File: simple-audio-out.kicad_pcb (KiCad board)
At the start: 2 copper layers, 49.5 x 72.4 mm, 12 parts, among them J1 Conn_01x04, Q1 2N3904

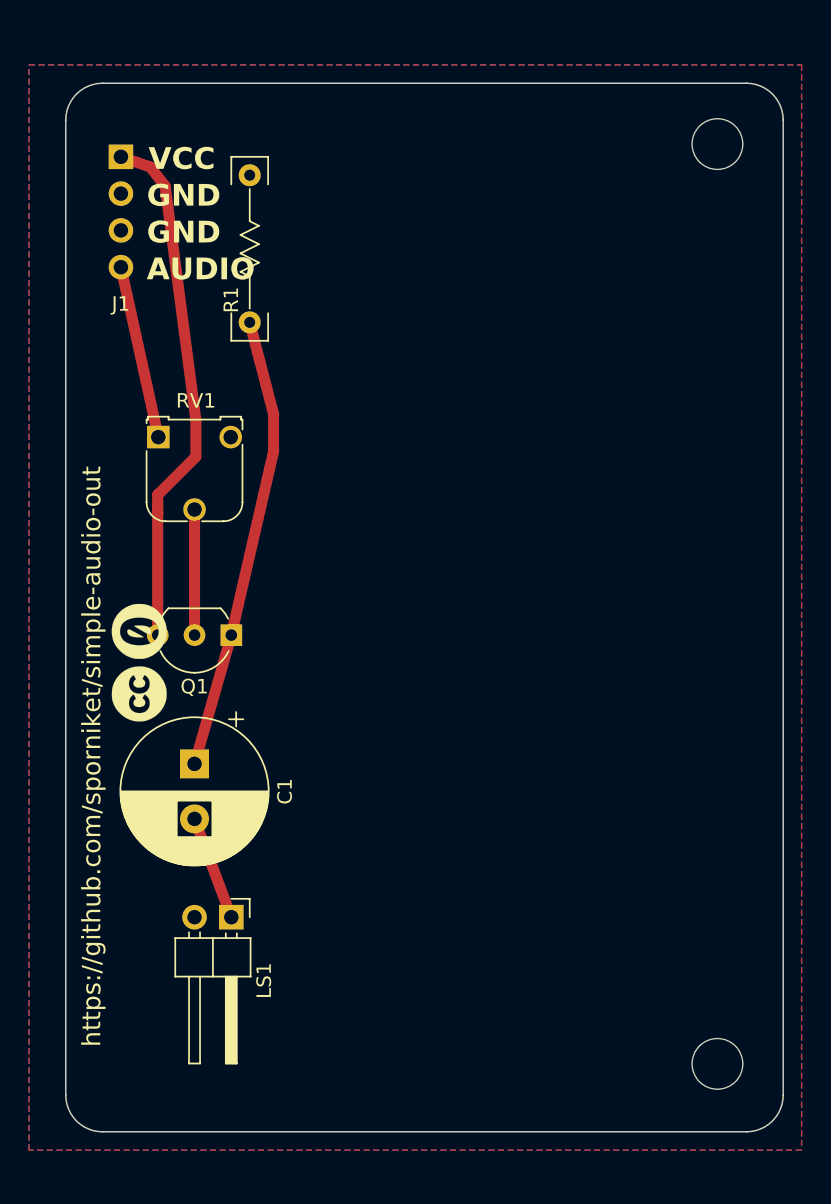
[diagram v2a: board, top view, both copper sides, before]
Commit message: #1 -- labels with project title, issue date, revision
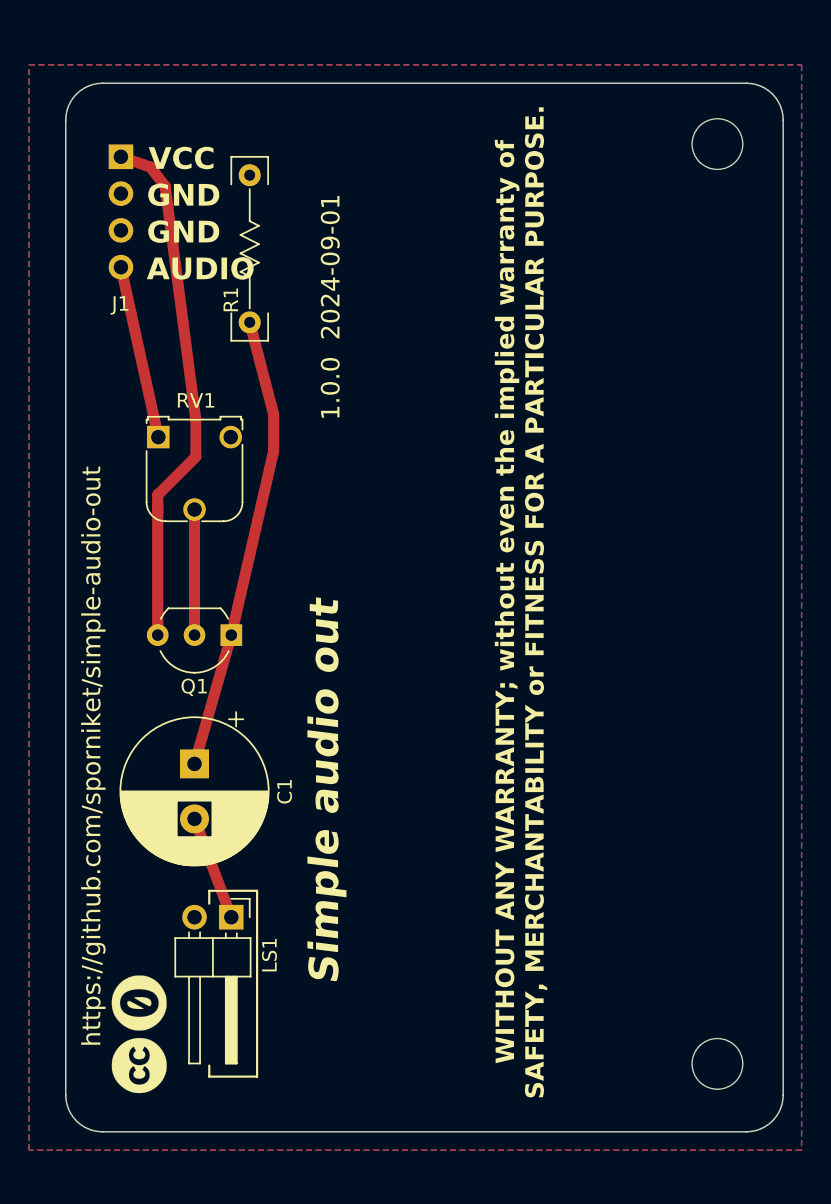
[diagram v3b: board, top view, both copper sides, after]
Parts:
- added G***: LOGO, cliparts:logo--cc--zero, B.Cu at (137.3, 55.6)
- added G***: LOGO, cliparts:logo--cc--cc, B.Cu at (137.2, 51.2)
- moved G*** 25.7 mm to (116.8, 86.9)
- moved G*** 25.7 mm to (116.8, 82.5)
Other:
- board text added: "${REVISION} ${ISSUE_DATE}"
- board text added: "${TITLE}"
